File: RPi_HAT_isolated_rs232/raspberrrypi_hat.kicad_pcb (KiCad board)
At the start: 4 copper layers, 65 x 56 mm, 70 parts, among them J1 Conn_01x06, J21 Conn_01x02, J22 Conn_01x05, J3 40HAT, J40 Conn_02x03_Odd_Even, J9 CONN_01X02, Q1 Q_PNP_BEC, Q39 Q_PNP_BEC, U2 CAT24C32, U21 DC-DC_CUI_PDQE20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

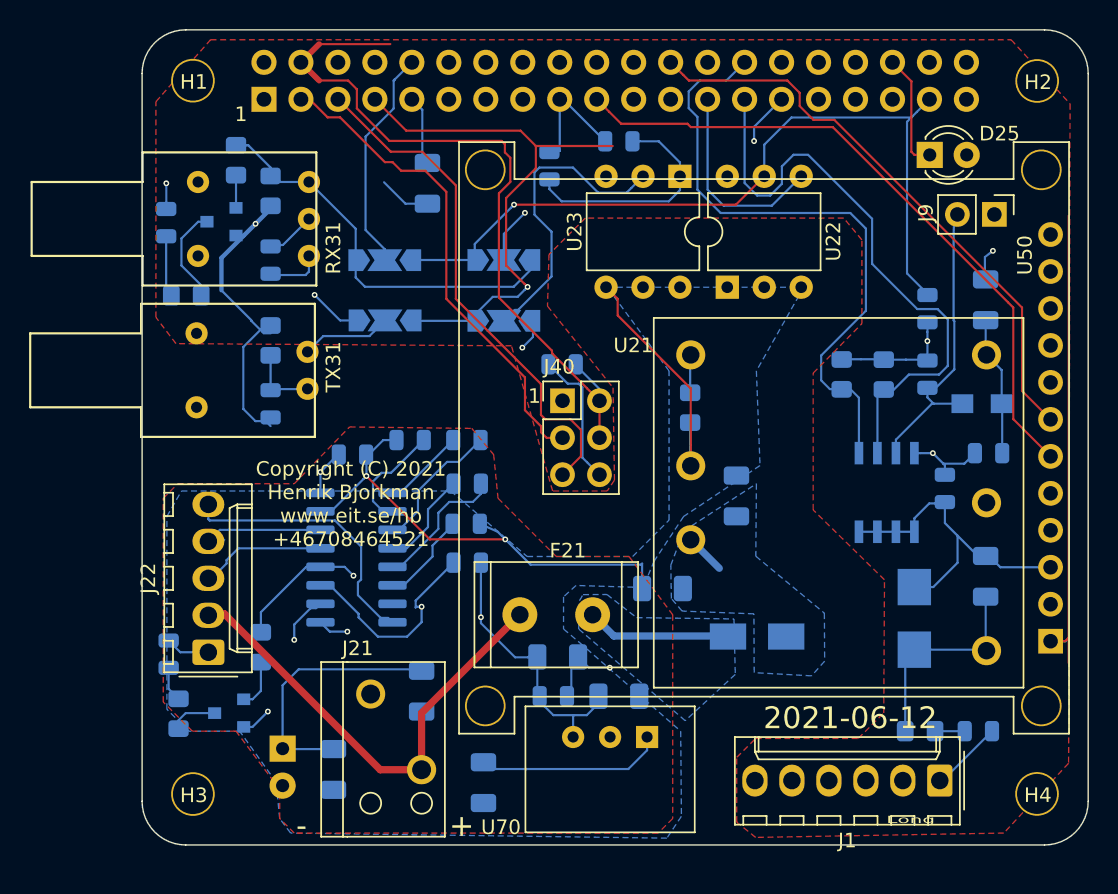
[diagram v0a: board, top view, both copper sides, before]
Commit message: This version was tested and something failed, see SuperCapUps7_rs232/bom.txt for details
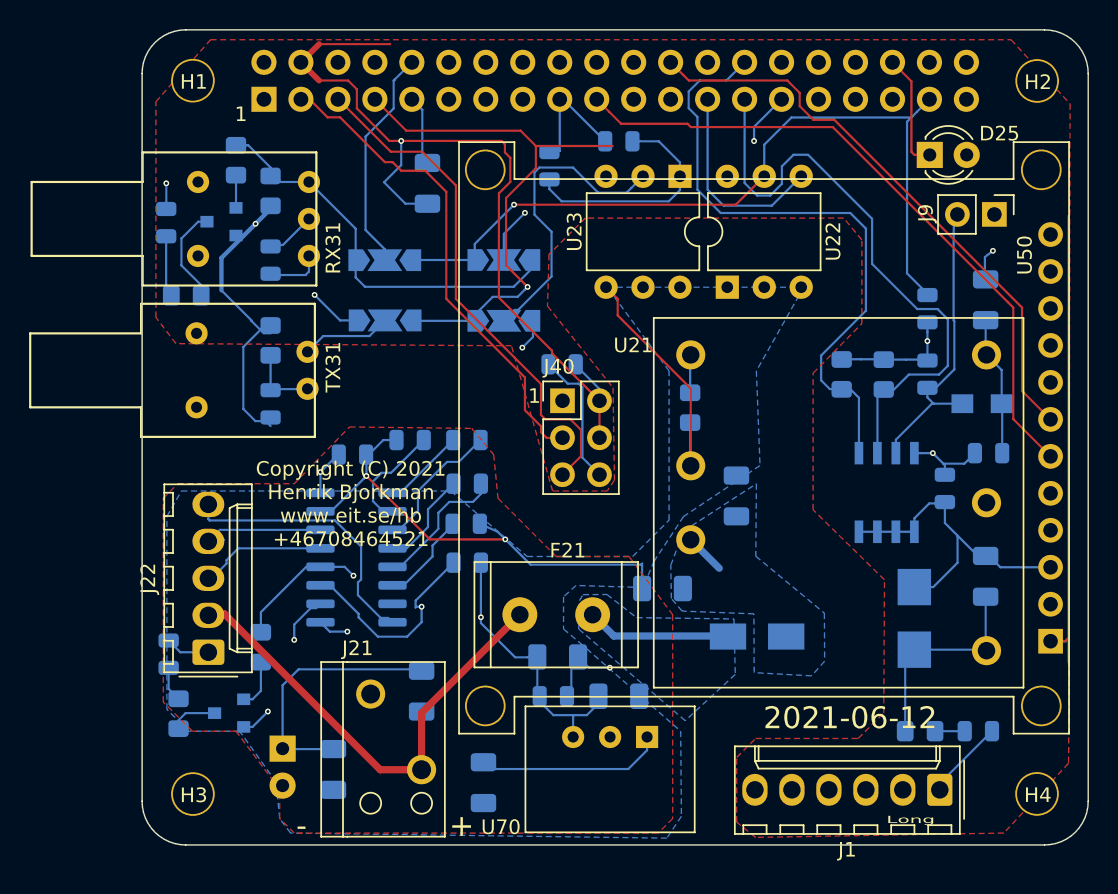
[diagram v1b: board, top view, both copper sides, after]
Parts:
- moved J1 0.64 mm to (133.3, 113.0)
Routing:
- net /P5V: track 109.1 -> 112.4 mm, vias 1 -> 2
- net /GPIO22_J1: track 72.1 -> 73.2 mm
- net /GPIO27_J1: track 74.1 -> 75.1 mm
- net GND: track 174.1 -> 174.8 mm
- net /GPIO23_J1: track 73.7 -> 74.4 mm
- net /GPIO17_J1: track 77.8 -> 78.4 mm
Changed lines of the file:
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@@
     (thickness 1.6)
     (drawings 74)
-    (tracks 723)
+    (tracks 731)
     (zones 0)
     (modules 70)
@@
   )
   (module Connector_Molex:Molex_KK-254_AE-6410-06A_1x06_P2.54mm_Vertical (layer F.Cu)
-    (at 133.35 112.395 180)
+    (at 133.35 113.03 180)
     (descr "Molex KK-254 Interconnect System, old/engineering part number: AE-6410-06A example for new part number: 22-27-2061, 6 Pins (http://www.molex.com/pdm_docs/sd/022272021_sd.pdf), generated with kicad-footprint-generator")
     (tags "connector Molex KK-254 side entry")
@@
   (segment (start 80.21 71.36) (end 80.21 73.115) (width 0.15) (layer B.Cu) (net 1))
   (segment (start 133.5425 112.395) (end 133.35 112.395) (width 0.15) (layer B.Cu) (net 1))
-  (segment (start 136.9375 109) (end 133.5425 112.395) (width 0.15) (layer B.Cu) (net 1))
+  (segment (start 133.35 112.5875) (end 133.35 113.03) (width 0.15) (layer B.Cu) (net 1))
+  (segment (start 136.9375 109) (end 133.35 112.5875) (width 0.15) (layer B.Cu) (net 1))
   (segment (start 129.065 85.96) (end 129.5 85.525) (width 0.15) (layer B.Cu) (net 2))
   (segment (start 129.065 89.9) (end 129.065 85.96) (width 0.15) (layer B.Cu) (net 2))
@@
   (segment (start 93.3 64.9) (end 93.3 66.21) (width 0.15) (layer F.Cu) (net 5))
   (segment (start 93.3 66.21) (end 95.54 68.45) (width 0.15) (layer F.Cu) (net 5))
-  (segment (start 95.54 68.45) (end 103.25 68.45) (width 0.15) (layer F.Cu) (net 5))
+  (segment (start 95.54 68.45) (end 96.35 68.45) (width 0.15) (layer F.Cu) (net 5))
   (segment (start 109.120001 85.450001) (end 109.97 86.3) (width 0.15) (layer F.Cu) (net 5))
   (segment (start 103.25 68.45) (end 103.47 68.67) (width 0.15) (layer F.Cu) (net 5))
@@
   (segment (start 130.975 104.025) (end 131.6 103.4) (width 0.15) (layer B.Cu) (net 5))
   (segment (start 130.975 109) (end 130.975 104.025) (width 0.15) (layer B.Cu) (net 5))
+  (segment (start 96.35 68.45) (end 103.25 68.45) (width 0.15) (layer F.Cu) (net 5))
+  (via (at 96.35 68.45) (size 0.4) (drill 0.2) (layers F.Cu B.Cu) (net 5))
+  (segment (start 96.35 70.11) (end 96.35 68.45) (width 0.15) (layer B.Cu) (net 5))
+  (segment (start 95.17 71.29) (end 96.35 70.11) (width 0.15) (layer B.Cu) (net 5))
   (segment (start 134.9 86.5) (end 132.925 86.5) (width 0.15) (layer B.Cu) (net 6))
   (segment (start 132.81 86.5) (end 130.335 88.975) (width 0.15) (layer B.Cu) (net 6))
@@
   (segment (start 121.29 70.88) (end 119.34 72.83) (width 0.15) (layer F.Cu) (net 22))
   (segment (start 119.34 72.83) (end 104.1 72.83) (width 0.15) (layer F.Cu) (net 22))
-  (segment (start 123.19 111.145) (end 123.19 112.395) (width 0.15) (layer In2.Cu) (net 23))
   (segment (start 99.62 65.59) (end 102.03 68) (width 0.15) (layer In2.Cu) (net 23))
   (segment (start 124.8 84.3) (end 124.8 93.7) (width 0.15) (layer In2.Cu) (net 23))
-  (segment (start 124.95999 109.37501) (end 123.19 111.145) (width 0.15) (layer In2.Cu) (net 23))
   (segment (start 102.03 68) (end 102.75 68) (width 0.15) (layer In2.Cu) (net 23))
   (segment (start 125.9 73.4) (end 129.249989 76.749989) (width 0.15) (layer In2.Cu) (net 23))
@@
   (segment (start 129.5 107.388924) (end 127.513914 109.37501) (width 0.15) (layer In2.Cu) (net 23))
   (segment (start 127.513914 109.37501) (end 124.95999 109.37501) (width 0.15) (layer In2.Cu) (net 23))
+  (segment (start 123.19 111.145) (end 123.19 113.03) (width 0.15) (layer In2.Cu) (net 23))
+  (segment (start 124.95999 109.37501) (end 123.19 111.145) (width 0.15) (layer In2.Cu) (net 23))
   (segment (start 108.348686 73) (end 102.16 66.811314) (width 0.15) (layer In2.Cu) (net 24))
   (segment (start 129.7 80.3) (end 129.7 76.5) (width 0.15) (layer In2.Cu) (net 24))
@@
   (segment (start 129.9 108.225) (end 129.9 98) (width 0.15) (layer In2.Cu) (net 24))
   (segment (start 126.2 73) (end 108.348686 73) (width 0.15) (layer In2.Cu) (net 24))
-  (segment (start 125.73 112.395) (end 129.9 108.225) (width 0.15) (layer In2.Cu) (net 24))
-  (segment (start 104.7 66.811314) (end 104.7 65.59) (width 0.15) (layer In2.Cu) (net 25))
-  (segment (start 108.849979 72.599979) (end 104.7 68.45) (width 0.15) (layer In2.Cu) (net 25))
-  (segment (start 130.1 76.3) (end 126.399979 72.599979) (width 0.15) (layer In2.Cu) (net 25))
-  (segment (start 130.1 80.9) (end 130.1 76.3) (width 0.15) (layer In2.Cu) (net 25))
-  (segment (start 126.399979 72.599979) (end 108.849979 72.599979) (width 0.15) (layer In2.Cu) (net 25))
-  (segment (start 125.8 85.2) (end 130.1 80.9) (width 0.15) (layer In2.Cu) (net 25))
-  (segment (start 125.8 93.1) (end 125.8 85.2) (width 0.15) (layer In2.Cu) (net 25))
-  (segment (start 104.7 68.45) (end 104.7 66.811314) (width 0.15) (layer In2.Cu) (net 25))
-  (segment (start 130.3 97.6) (end 125.8 93.1) (width 0.15) (layer In2.Cu) (net 25))
-  (segment (start 130.3 110.135) (end 130.3 97.6) (width 0.15) (layer In2.Cu) (net 25))
-  (segment (start 128.27 112.165) (end 130.3 110.135) (width 0.15) (layer In2.Cu) (net 25))
+  (segment (start 125.73 111.78) (end 125.73 113.03) (width 0.15) (layer In2.Cu) (net 24))
+  (segment (start 129.285 108.225) (end 125.73 111.78) (width 0.15) (layer In2.Cu) (net 24))
+  (segment (start 129.9 108.225) (end 129.285 108.225) (width 0.15) (layer In2.Cu) (net 24))
   (segment (start 128.27 112.395) (end 128.27 112.165) (width 0.15) (layer In2.Cu) (net 25))
-  (segment (start 109.4 72.15) (end 106 68.75) (width 0.15) (layer In2.Cu) (net 26))
-  (segment (start 130.6 76.1) (end 126.65 72.15) (width 0.15) (layer In2.Cu) (net 26))
-  (segment (start 105.563599 63.913599) (end 104.7 63.05) (width 0.15) (layer In2.Cu) (net 26))
-  (segment (start 130.6 81.4) (end 130.6 76.1) (width 0.15) (layer In2.Cu) (net 26))
-  (segment (start 126.4 85.6) (end 130.6 81.4) (width 0.15) (layer In2.Cu) (net 26))
-  (segment (start 106 68.75) (end 106 64.35) (width 0.15) (layer In2.Cu) (net 26))
-  (segment (start 126.4 92.8) (end 126.4 85.6) (width 0.15) (layer In2.Cu) (net 26))
-  (segment (start 106 64.35) (end 105.563599 63.913599) (width 0.15) (layer In2.Cu) (net 26))
-  (segment (start 126.65 72.15) (end 109.4 72.15) (width 0.15) (layer In2.Cu) (net 26))
-  (segment (start 130.81 97.21) (end 126.4 92.8) (width 0.15) (layer In2.Cu) (net 26))
-  (segment (start 130.81 112.395) (end 130.81 97.21) (width 0.15) (layer In2.Cu) (net 26))
+  (segment (start 128.27 111.78) (end 128.27 113.03) (width 0.15) (layer In2.Cu) (net 25))
+  (segment (start 129.915 110.135) (end 128.27 111.78) (width 0.15) (layer In2.Cu) (net 25))
+  (segment (start 130.3 110.135) (end 129.915 110.135) (width 0.15) (layer In2.Cu) (net 25))
+  (segment (start 130.3 97.6) (end 130.3 110.135) (width 0.15) (layer In2.Cu) (net 25))
+  (segment (start 125.8 93.1) (end 130.3 97.6) (width 0.15) (layer In2.Cu) (net 25))
+  (segment (start 130.1 80.9) (end 125.8 85.2) (width 0.15) (layer In2.Cu) (net 25))
+  (segment (start 125.8 85.2) (end 125.8 93.1) (width 0.15) (layer In2.Cu) (net 25))
+  (segment (start 126.399979 72.599979) (end 130.1 76.3) (width 0.15) (layer In2.Cu) (net 25))
+  (segment (start 130.1 76.3) (end 130.1 80.9) (width 0.15) (layer In2.Cu) (net 25))
+  (segment (start 104.7 68.45) (end 108.849979 72.599979) (width 0.15) (layer In2.Cu) (net 25))
+  (segment (start 108.849979 72.599979) (end 126.399979 72.599979) (width 0.15) (layer In2.Cu) (net 25))
+  (segment (start 104.7 65.59) (end 104.7 68.45) (width 0.15) (layer In2.Cu) (net 25))
+  (segment (start 130.81 107.79) (end 130.81 113.03) (width 0.15) (layer In2.Cu) (net 26))
+  (segment (start 126.4 92.8) (end 130.81 97.21) (width 0.15) (layer In2.Cu) (net 26))
+  (segment (start 126.4 85.6) (end 126.4 92.8) (width 0.15) (layer In2.Cu) (net 26))
+  (segment (start 130.6 81.4) (end 126.4 85.6) (width 0.15) (layer In2.Cu) (net 26))
+  (segment (start 130.6 76.1) (end 130.6 81.4) (width 0.15) (layer In2.Cu) (net 26))
+  (segment (start 109.4 72.15) (end 126.65 72.15) (width 0.15) (layer In2.Cu) (net 26))
+  (segment (start 130.81 97.21) (end 130.81 107.79) (width 0.15) (layer In2.Cu) (net 26))
+  (segment (start 106 68.75) (end 109.4 72.15) (width 0.15) (layer In2.Cu) (net 26))
+  (segment (start 126.65 72.15) (end 130.6 76.1) (width 0.15) (layer In2.Cu) (net 26))
+  (segment (start 106 64.35) (end 106 68.75) (width 0.15) (layer In2.Cu) (net 26))
+  (segment (start 104.7 63.05) (end 106 64.35) (width 0.15) (layer In2.Cu) (net 26))
   (segment (start 116.2 83.19) (end 116.24 83.15) (width 0.15) (layer B.Cu) (net 27))
   (segment (start 116.2 85.75) (end 116.2 83.19) (width 0.15) (layer B.Cu) (net 27))
